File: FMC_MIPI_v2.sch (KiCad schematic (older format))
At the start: 0 parts

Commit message: minor changes 4
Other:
- note added: "Power requirements: \nVOLT_2P5 -> 0.5 A\n"
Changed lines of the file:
@@
 $Descr A4 11693 8268
 encoding utf-8
-Sheet 1 10
+Sheet 1 11
 Title ""
 Date ""
@@
 F0 "Jetson_connector" 50
 F1 "Jetson_connector.sch" 50
-F2 "VOLT_1P8" I L 7700 3000 50
+F2 "VOLT_1P8" I L 7700 3050 50
+F3 "VDD_VADJ" I L 7700 2950 50
 $EndSheet
-$Comp
-L FMC_MIPI_v2:Earth #PWR01
-U 1 1 61B01356
-P 5950 5600
-F 0 "#PWR01" H 5950 5350 50  0001 C CNN
-F 1 "Earth" H 5950 5450 50  0001 C CNN
-F 2 "" H 5950 5600 50  0001 C CNN
-F 3 "~" H 5950 5600 50  0001 C CNN
-	1    5950 5600
-	1    0    0    -1
-$EndComp
 Text Notes 6850 5350 0    50   ~ 0
 PI3WVR646 is 10 lines!!! use it!! when available\n\nPI3WVR626	PI3WVR626 Datasheet	2:1 MIPI 2-Data Lane, 1.5Gbps(D-PHY) Switch\nPI3WVR628	PI3WVR628 Datasheet	2:1 MIPI 2-Data Lane, 4.5Gbps(D-PHY) switch\nPI3WVR646	PI3WVR646 Datasheet	2:1 MIPI 4-Data Lane, 2.5Gbps(D-PHY) Switch\nPI3WVR648	PI3WVR648 Product brief	2:1 MIPI 4-Data Lane, 4.5Gbps(D-PHY) Switch\n		\n\n\n\nConsider using SNx5DPHY440SS retimer (no stock)
@@
 F5 "VOLT_3P3" I L 1150 3300 50
 $EndSheet
-Text Notes 1450 4650 0    50   ~ 0
+Text Notes 900  4450 0    50   ~ 0
 TODO: check level switching  with FPGA when OE and DIR are tied to ground without resistor
-Text Notes 1450 5250 0    50   ~ 0
+Text Notes 900  4600 0    50   ~ 0
 For I2C level shifting we will use TCA9406DCUR
 Text Notes -100 -400 0    118  ~ 0
 To switch cameras simply use: TS5MP645\n\nhttps://www.ti.com/lit/ds/symlink/ts5mp645.pdf?ts=1639239156409&ref_url=https%253A%252F%252Fwww.ti.com%252Fproduct%252FTS5MP645
-Text Notes 1450 5750 0    50   ~ 0
+Text Notes 900  4700 0    50   ~ 0
 Add another solution using PI3WVR646 or similar switch
-Text Notes 1450 6050 0    50   ~ 0
+Text Notes 900  4900 0    50   ~ 0
 For low power (LP) lines use only one livel shifter, and connect the output to multiple\nswitches. If needed, merge to pins to get more power.
 Text Notes 4100 1850 0    118  ~ 24
@@
 Text Notes 3450 3100 0    79   ~ 0
 TODO!!! Add 1.8 level shifter to interface the jetson pins!!!
+$Sheet
+S 1000 5300 3100 1150
+U 6362ECC5
+F0 "Slow_signals_level_shifters" 50
+F1 "Slow_signals_level_shifters.sch" 50
+F2 "VDD_VADJ" I L 1000 5400 50
+F3 "VOLT_1P8" I L 1000 5500 50
+$EndSheet
+Wire Notes Line
+	500  6900 2500 6900
+Wire Notes Line
+	2500 6900 2500 7800
+Text Notes 550  7100 0    50   ~ 0
+Power requirements: \nVOLT_2P5 -> 0.5 A\n
 $EndSCHEMATC

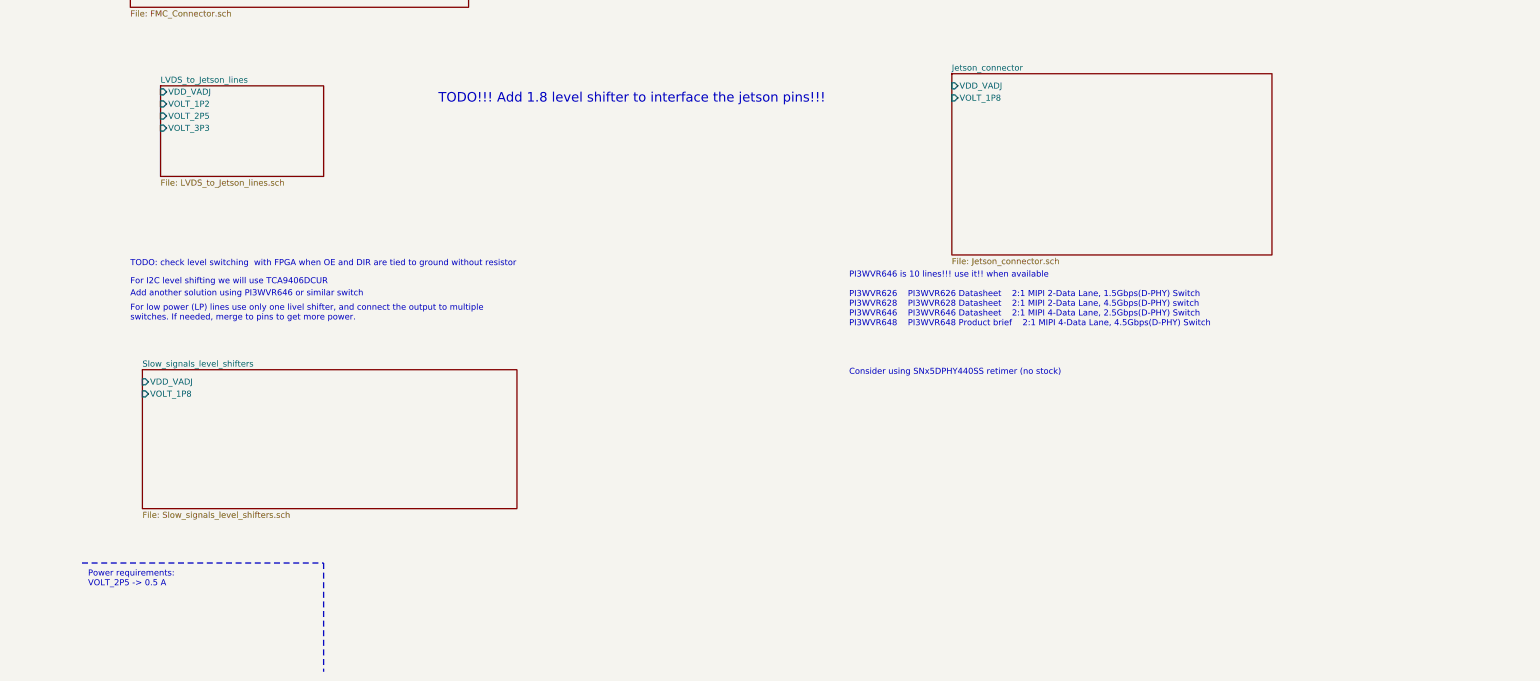
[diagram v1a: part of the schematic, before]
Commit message: adding power supplies
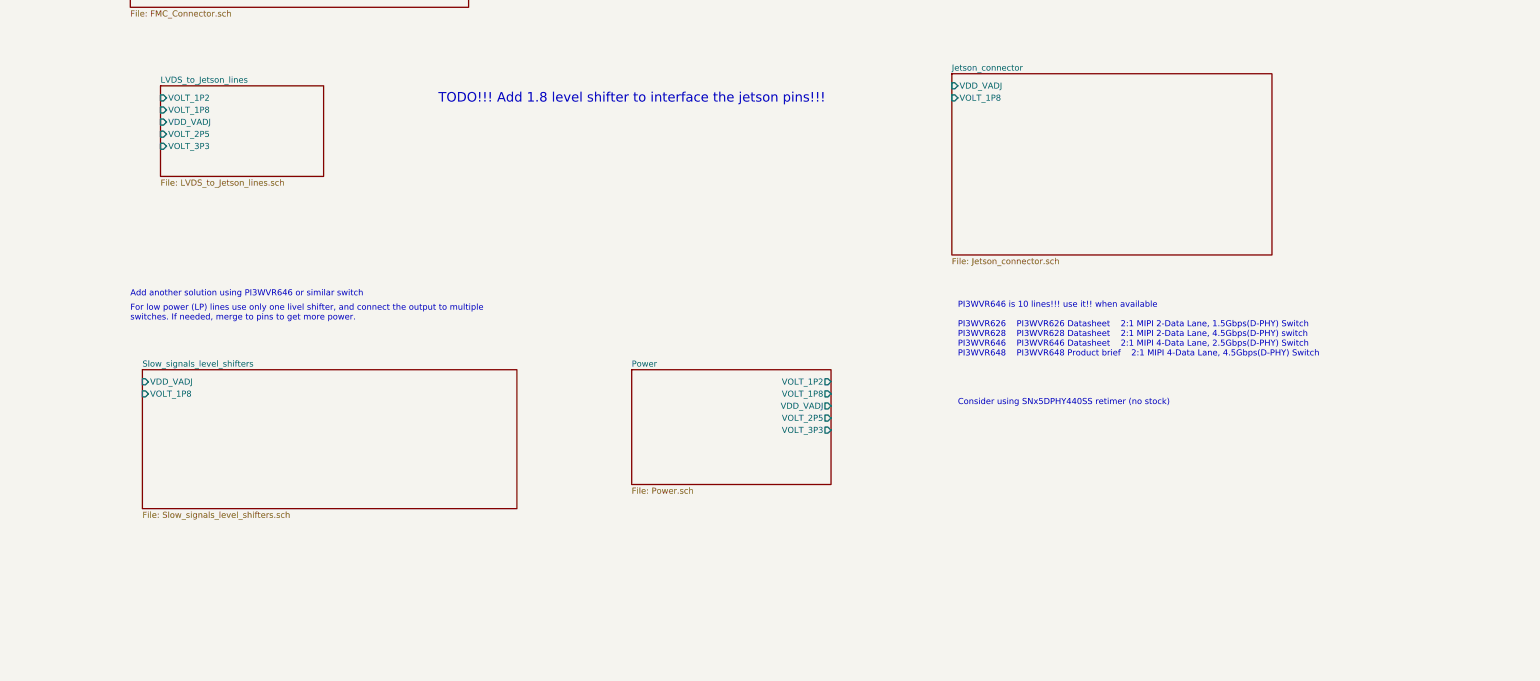
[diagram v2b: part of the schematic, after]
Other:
- note removed: "For I2C level shifting we will use TCA9406DCUR"
- note removed: "Power requirements: \nVOLT_2P5 -> 0.5 A\n"
- note removed: "TODO: check level switching with FPGA when OE and DIR are tied to ground without resistor"
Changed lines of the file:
@@
 $Descr A4 11693 8268
 encoding utf-8
-Sheet 1 11
+Sheet 1 12
 Title ""
 Date ""
@@
 F3 "VDD_VADJ" I L 7700 2950 50
 $EndSheet
-Text Notes 6850 5350 0    50   ~ 0
+Text Notes 7750 5600 0    50   ~ 0
 PI3WVR646 is 10 lines!!! use it!! when available\n\nPI3WVR626	PI3WVR626 Datasheet	2:1 MIPI 2-Data Lane, 1.5Gbps(D-PHY) Switch\nPI3WVR628	PI3WVR628 Datasheet	2:1 MIPI 2-Data Lane, 4.5Gbps(D-PHY) switch\nPI3WVR646	PI3WVR646 Datasheet	2:1 MIPI 4-Data Lane, 2.5Gbps(D-PHY) Switch\nPI3WVR648	PI3WVR648 Product brief	2:1 MIPI 4-Data Lane, 4.5Gbps(D-PHY) Switch\n		\n\n\n\nConsider using SNx5DPHY440SS retimer (no stock)
 $Sheet
@@
 F0 "LVDS_to_Jetson_lines" 50
 F1 "LVDS_to_Jetson_lines.sch" 50
-F2 "VDD_VADJ" I L 1150 3000 50
-F3 "VOLT_1P2" I L 1150 3100 50
-F4 "VOLT_2P5" I L 1150 3200 50
-F5 "VOLT_3P3" I L 1150 3300 50
+F2 "VDD_VADJ" I L 1150 3250 50
+F3 "VOLT_1P2" I L 1150 3050 50
+F4 "VOLT_2P5" I L 1150 3350 50
+F5 "VOLT_3P3" I L 1150 3450 50
+F6 "VOLT_1P8" I L 1150 3150 50
 $EndSheet
-Text Notes 900  4450 0    50   ~ 0
-TODO: check level switching  with FPGA when OE and DIR are tied to ground without resistor
-Text Notes 900  4600 0    50   ~ 0
-For I2C level shifting we will use TCA9406DCUR
 Text Notes -100 -400 0    118  ~ 0
 To switch cameras simply use: TS5MP645\n\nhttps://www.ti.com/lit/ds/symlink/ts5mp645.pdf?ts=1639239156409&ref_url=https%253A%252F%252Fwww.ti.com%252Fproduct%252FTS5MP645
@@
 F3 "VOLT_1P8" I L 1000 5500 50
 $EndSheet
-Wire Notes Line
-	500  6900 2500 6900
-Wire Notes Line
-	2500 6900 2500 7800
-Text Notes 550  7100 0    50   ~ 0
-Power requirements: \nVOLT_2P5 -> 0.5 A\n
+$Sheet
+S 5050 5300 1650 950
+U 637747EF
+F0 "Power" 50
+F1 "Power.sch" 50
+F2 "VDD_VADJ" O R 6700 5600 50
+F3 "VOLT_1P2" O R 6700 5400 50
+F4 "VOLT_2P5" O R 6700 5700 50
+F5 "VOLT_3P3" O R 6700 5800 50
+F6 "VOLT_1P8" O R 6700 5500 50
+$EndSheet
 $EndSCHEMATC

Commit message: adding more power supplies
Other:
- note added: "For direct convertion BLVDS to SLVS we will use 9.1 Ohm resistor .Oct 10, 2022"
- note removed: "Looks like we need 15 Ohm resistor after re-driver!!! With 12 Ohm the swing is only 115 mVolt!!!\n\nCheck it!!!\n\nFor direct convertion BLVDS to SLVS we will use 9.1 Ohm resistor .Oct 10, 2022"
- note removed: "TODO!!! Add 1.8 level shifter to interface the jetson pins!!!"
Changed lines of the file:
@@
 $EndDescr
 $Sheet
-S 900  850  2800 1450
+S 700  900  1300 800
 U 6170B975
 F0 "FMC_Connector" 50
 F1 "FMC_Connector.sch" 50
+F2 "VDD_VADJ" O R 2000 1050 50
+F3 "VOLT_3P3" O R 2000 1150 50
 $EndSheet
 $Sheet
-S 7700 2850 2650 1500
+S 4950 2500 1450 750
 U 61ACA102
 F0 "Jetson_connector" 50
 F1 "Jetson_connector.sch" 50
-F2 "VOLT_1P8" I L 7700 3050 50
-F3 "VDD_VADJ" I L 7700 2950 50
+F2 "VOLT_1P8" I L 4950 2700 50
+F3 "VDD_VADJ" I L 4950 2600 50
 $EndSheet
 Text Notes 7750 5600 0    50   ~ 0
 PI3WVR646 is 10 lines!!! use it!! when available\n\nPI3WVR626	PI3WVR626 Datasheet	2:1 MIPI 2-Data Lane, 1.5Gbps(D-PHY) Switch\nPI3WVR628	PI3WVR628 Datasheet	2:1 MIPI 2-Data Lane, 4.5Gbps(D-PHY) switch\nPI3WVR646	PI3WVR646 Datasheet	2:1 MIPI 4-Data Lane, 2.5Gbps(D-PHY) Switch\nPI3WVR648	PI3WVR648 Product brief	2:1 MIPI 4-Data Lane, 4.5Gbps(D-PHY) Switch\n		\n\n\n\nConsider using SNx5DPHY440SS retimer (no stock)
 $Sheet
-S 1150 2950 1350 750
+S 5800 950  1300 950
 U 6191D89C
 F0 "LVDS_to_Jetson_lines" 50
 F1 "LVDS_to_Jetson_lines.sch" 50
-F2 "VDD_VADJ" I L 1150 3250 50
-F3 "VOLT_1P2" I L 1150 3050 50
-F4 "VOLT_2P5" I L 1150 3350 50
-F5 "VOLT_3P3" I L 1150 3450 50
-F6 "VOLT_1P8" I L 1150 3150 50
+F2 "VDD_VADJ" I L 5800 1050 50
+F3 "VOLT_1P2" I L 5800 1350 50
+F4 "VOLT_2P5" I L 5800 1450 50
+F5 "VOLT_3P3" I L 5800 1150 50
 $EndSheet
 Text Notes -100 -400 0    118  ~ 0
@@
 Text Notes 900  4900 0    50   ~ 0
 For low power (LP) lines use only one livel shifter, and connect the output to multiple\nswitches. If needed, merge to pins to get more power.
-Text Notes 4100 1850 0    118  ~ 24
-Looks like we need 15 Ohm resistor after re-driver!!! With 12 Ohm the swing is only 115 mVolt!!!\n\nCheck it!!!\n\nFor direct convertion BLVDS to SLVS we will use 9.1 Ohm resistor .Oct 10, 2022
-Text Notes 3450 3100 0    79   ~ 0
-TODO!!! Add 1.8 level shifter to interface the jetson pins!!!
+Text Notes -200 -1200 0    118  ~ 24
+For direct convertion BLVDS to SLVS we will use 9.1 Ohm resistor .Oct 10, 2022
 $Sheet
-S 1000 5300 3100 1150
+S 1350 2500 1300 800
 U 6362ECC5
 F0 "Slow_signals_level_shifters" 50
 F1 "Slow_signals_level_shifters.sch" 50
-F2 "VDD_VADJ" I L 1000 5400 50
-F3 "VOLT_1P8" I L 1000 5500 50
+F2 "VDD_VADJ" I L 1350 2600 50
+F3 "VOLT_1P8" I L 1350 2700 50
 $EndSheet
 $Sheet
-S 5050 5300 1650 950
+S 2600 950  1650 950
 U 637747EF
 F0 "Power" 50
 F1 "Power.sch" 50
-F2 "VDD_VADJ" O R 6700 5600 50
-F3 "VOLT_1P2" O R 6700 5400 50
-F4 "VOLT_2P5" O R 6700 5700 50
-F5 "VOLT_3P3" O R 6700 5800 50
-F6 "VOLT_1P8" O R 6700 5500 50
+F2 "VOLT_1P2" O R 4250 1050 50
+F3 "VOLT_2P5" O R 4250 1250 50
+F4 "VOLT_1P8" O R 4250 1150 50
+F5 "VDD_VADJ" I L 2600 1050 50
+F6 "VOLT_3P3" I L 2600 1150 50
 $EndSheet
+Wire Wire Line
+	2000 1050 2600 1050
+Wire Wire Line
+	2000 1150 2600 1150
+Text Label 2150 1050 0    50   ~ 0
+VDD_VADJ
+Text Label 2150 1150 0    50   ~ 0
+VOLT_3P3
+Wire Wire Line
+	5800 1150 5300 1150
+Text Label 5300 1150 0    50   ~ 0
+VOLT_3P3
+Wire Wire Line
+	5800 1050 5300 1050
+Text Label 5300 1050 0    50   ~ 0
+VDD_VADJ
+Wire Wire Line
+	4250 1050 4550 1050
+Wire Wire Line
+	4250 1150 4550 1150
+Wire Wire Line
+	4250 1250 4550 1250
+Text Label 4550 1050 0    50   ~ 0
+VOLT_1P2
+Text Label 4550 1150 0    50   ~ 0
+VOLT_1P8
+Text Label 4550 1250 0    50   ~ 0
+VOLT_2P5
+Wire Wire Line
+	4950 2600 4400 2600
+Wire Wire Line
+	4950 2700 4400 2700
+Wire Wire Line
+	5800 1350 5300 1350
+Wire Wire Line
+	5800 1450 5300 1450
+Text Label 5300 1350 0    50   ~ 0
+VOLT_1P2
+Text Label 5300 1450 0    50   ~ 0
+VOLT_2P5
+Text Label 4400 2600 0    50   ~ 0
+VDD_VADJ
+Text Label 4400 2700 0    50   ~ 0
+VOLT_1P8
+Wire Wire Line
+	1350 2600 800  2600
+Wire Wire Line
+	1350 2700 800  2700
+Text Label 800  2600 0    50   ~ 0
+VDD_VADJ
+Text Label 800  2700 0    50   ~ 0
+VOLT_1P8
 $EndSCHEMATC

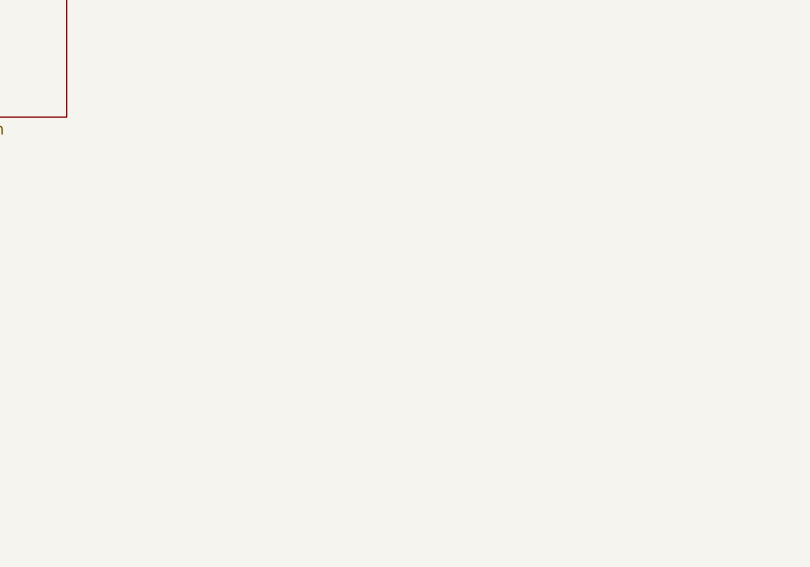
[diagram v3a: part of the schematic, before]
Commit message: Adding more LVDS lines
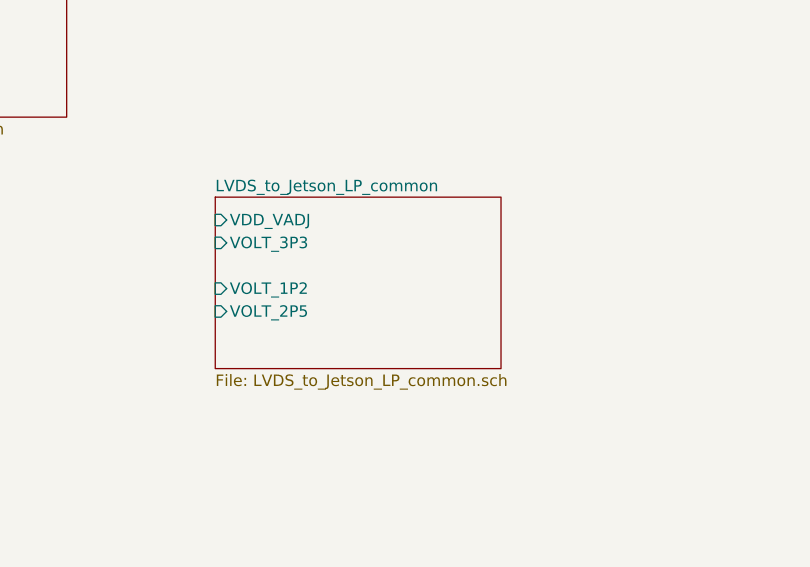
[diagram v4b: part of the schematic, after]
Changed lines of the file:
@@
 $Descr A4 11693 8268
 encoding utf-8
-Sheet 1 12
+Sheet 1 19
 Title ""
 Date ""
@@
 Text Label 800  2700 0    50   ~ 0
 VOLT_1P8
+$Sheet
+S 7750 2250 1250 750
+U 6366AF3A
+F0 "LVDS_to_Jetson_LP_common" 50
+F1 "LVDS_to_Jetson_LP_common.sch" 50
+F2 "VDD_VADJ" I L 7750 2350 50
+F3 "VOLT_1P2" I L 7750 2650 50
+F4 "VOLT_2P5" I L 7750 2750 50
+F5 "VOLT_3P3" I L 7750 2450 50
+$EndSheet
 $EndSCHEMATC

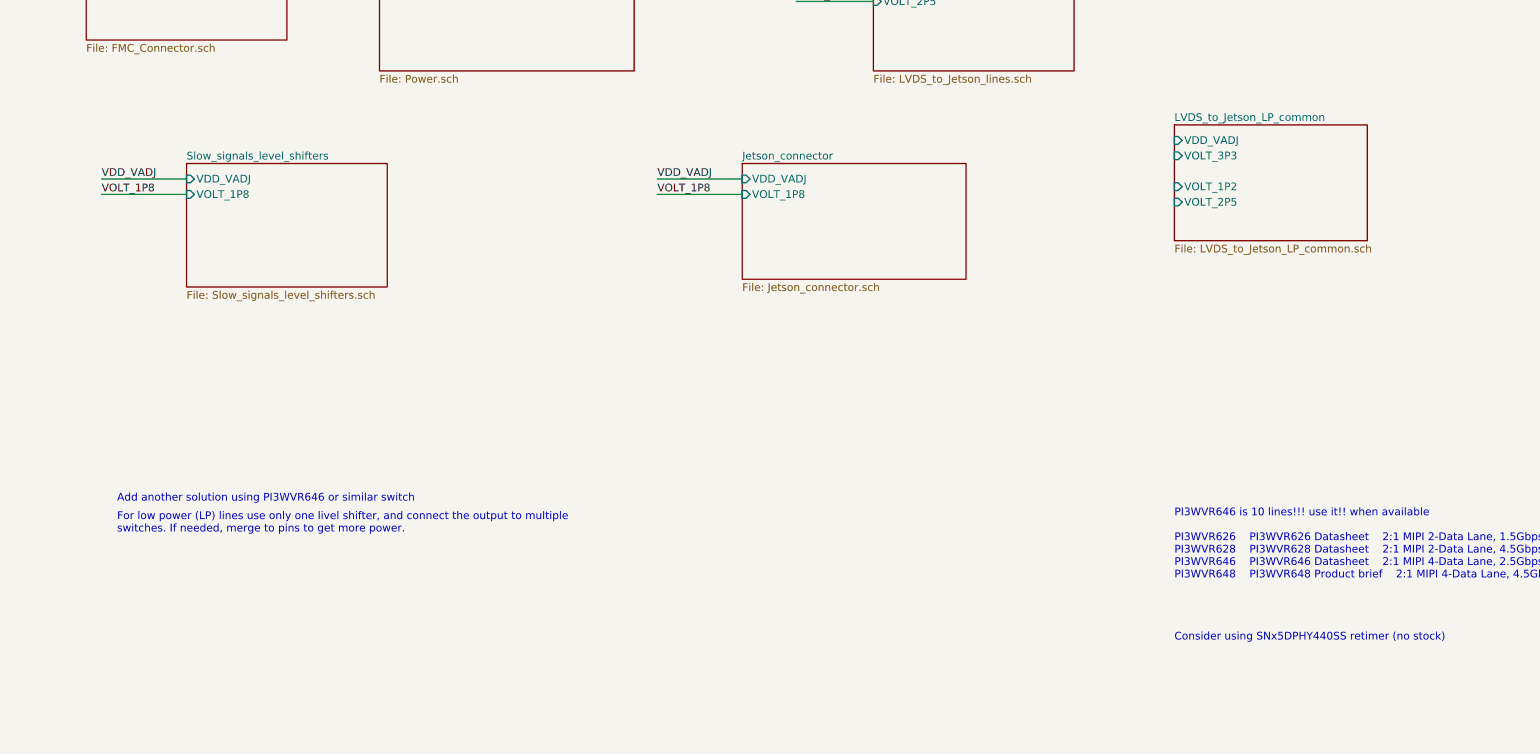
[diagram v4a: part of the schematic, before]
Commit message: added 4 bit level shifter VADJ to 3.3 volt
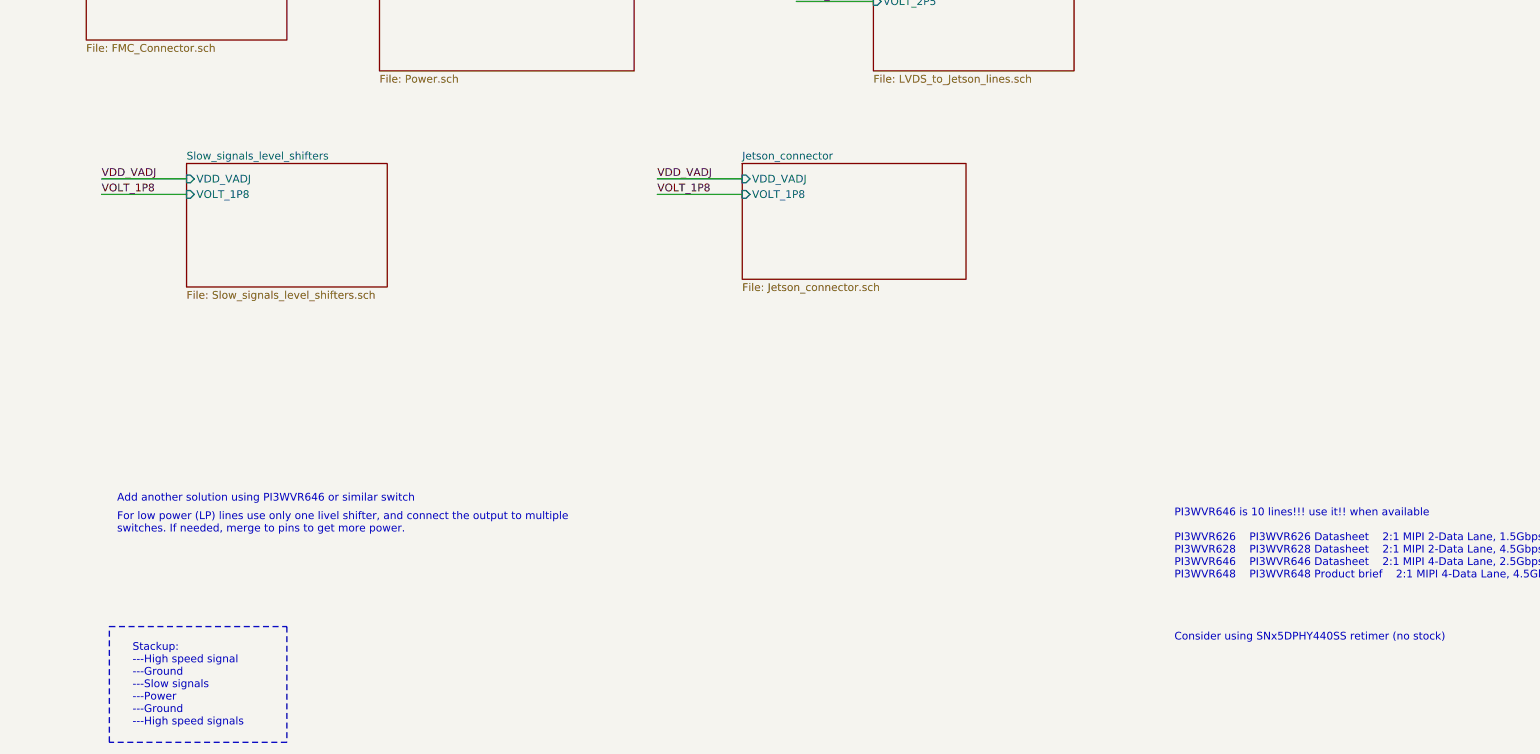
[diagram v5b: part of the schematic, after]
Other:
- note added: "Stackup:\n---High speed signal\n---Ground\n---Slow signals\n---Power\n---Ground\n---High speed signals"
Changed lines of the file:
@@
 $Descr A4 11693 8268
 encoding utf-8
-Sheet 1 19
+Sheet 1 12
 Title ""
 Date ""
@@
 Text Label 800  2700 0    50   ~ 0
 VOLT_1P8
-$Sheet
-S 7750 2250 1250 750
-U 6366AF3A
-F0 "LVDS_to_Jetson_LP_common" 50
-F1 "LVDS_to_Jetson_LP_common.sch" 50
-F2 "VDD_VADJ" I L 7750 2350 50
-F3 "VOLT_1P2" I L 7750 2650 50
-F4 "VOLT_2P5" I L 7750 2750 50
-F5 "VOLT_3P3" I L 7750 2450 50
-$EndSheet
+Text Notes 1000 6150 0    50   ~ 0
+Stackup:\n---High speed signal\n---Ground\n---Slow signals\n---Power\n---Ground\n---High speed signals
+Wire Notes Line
+	850  5500 2000 5500
+Wire Notes Line
+	2000 5500 2000 6250
+Wire Notes Line
+	2000 6250 850  6250
+Wire Notes Line
+	850  6250 850  5500
 $EndSCHEMATC
